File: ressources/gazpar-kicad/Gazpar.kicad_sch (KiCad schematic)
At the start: 9 parts, among them J1 Alim, U1 PC817, U2 ESP-01S, U3 AMS1117

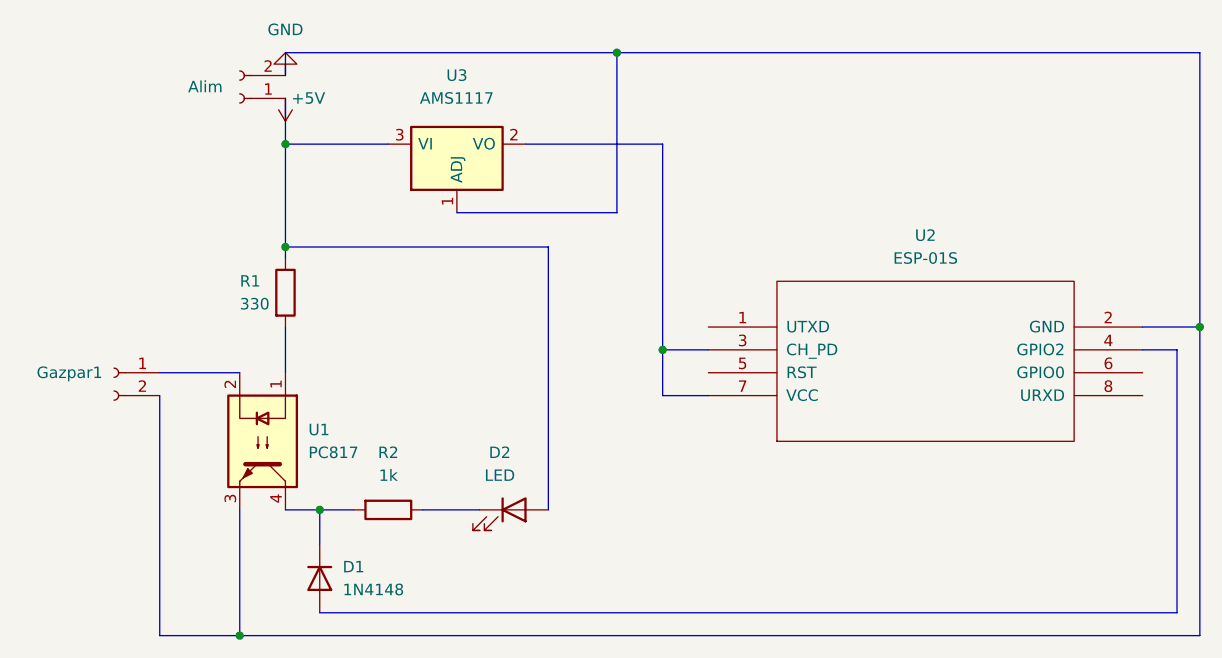
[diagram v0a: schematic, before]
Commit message: doc(gazpar): move from esp01 to esp32
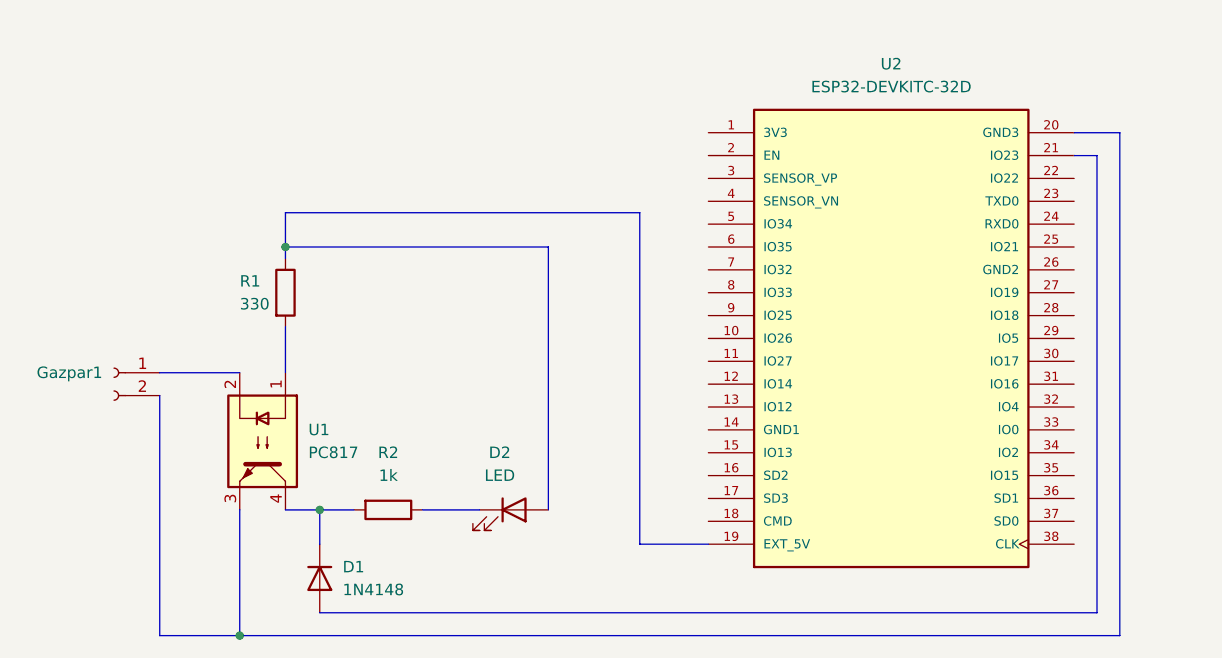
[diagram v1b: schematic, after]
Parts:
- removed J1: Alim, Connector_PinHeader_2.54mm:PinHeader_1x02_P2.54mm_Vertical, symbol Connector:Conn_01x02_Female
- removed U2: ESP-01S, ESP8266:ESP-01, symbol ESP8266:ESP-01v090
- removed U3: AMS1117, Connector_PinHeader_2.54mm:PinHeader_1x03_P2.54mm_Vertical, symbol Regulator_Linear:AMS1117
- added U2: ESP32-DEVKITC-32D, MODULE_ESP32-DEVKITC-32D, symbol ESP32-DEVKITC-32D:ESP32-DEVKITC-32D
- Gazpar1: footprint Connector_PinHeader_2.54mm:PinHeader_1x02_P2.54mm_Vertical -> TerminalBlock:TerminalBlock_bornier-2_P5.08mm
- R1, R2: footprint Resistor_THT:R_Axial_DIN0309_L9.0mm_D3.2mm_P2.54mm_Vertical -> Resistor_THT:R_Axial_DIN0207_L6.3mm_D2.5mm_P7.62mm_Horizontal
